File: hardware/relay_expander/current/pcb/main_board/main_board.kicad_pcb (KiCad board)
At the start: 2 copper layers, 100 x 85 mm, 105 parts, among them J1 Conn_01x07_Socket, J10 Screw_Terminal_01x02, J11 Screw_Terminal_01x02, J12 Screw_Terminal_01x02, J13 Screw_Terminal_01x02, J14 Screw_Terminal_01x02, J15 Screw_Terminal_01x02, J2 Conn_01x07_Socket, J3 Screw_Terminal_01x02, J4 Screw_Terminal_01x02, J5 Screw_Terminal_01x02, J6 Screw_Terminal_01x02, J7 Screw_Terminal_01x02, J8 Screw_Terminal_01x03, J9 Screw_Terminal_01x02, K1 HF46F-12-HS1, K2 HF46F-12-HS1, K3 HF46F-12-HS1, K4 HF46F-12-HS1, K5 HF46F-12-HS1, K6 HF46F-12-HS1, K7 HF46F-12-HS1, K8 HF46F-12-HS1, Q1 BC548, Q2 BC548, Q3 BC548, Q4 BC548, Q5 BC548, Q6 BC548, Q7 BC548, Q8 BC548, SW1 SW_DIP_x03, U1 MCP23017x-x-SO, U2 TCMT4100, U3 TCMT4100, U4 TCMT4100, U5 TCMT4100

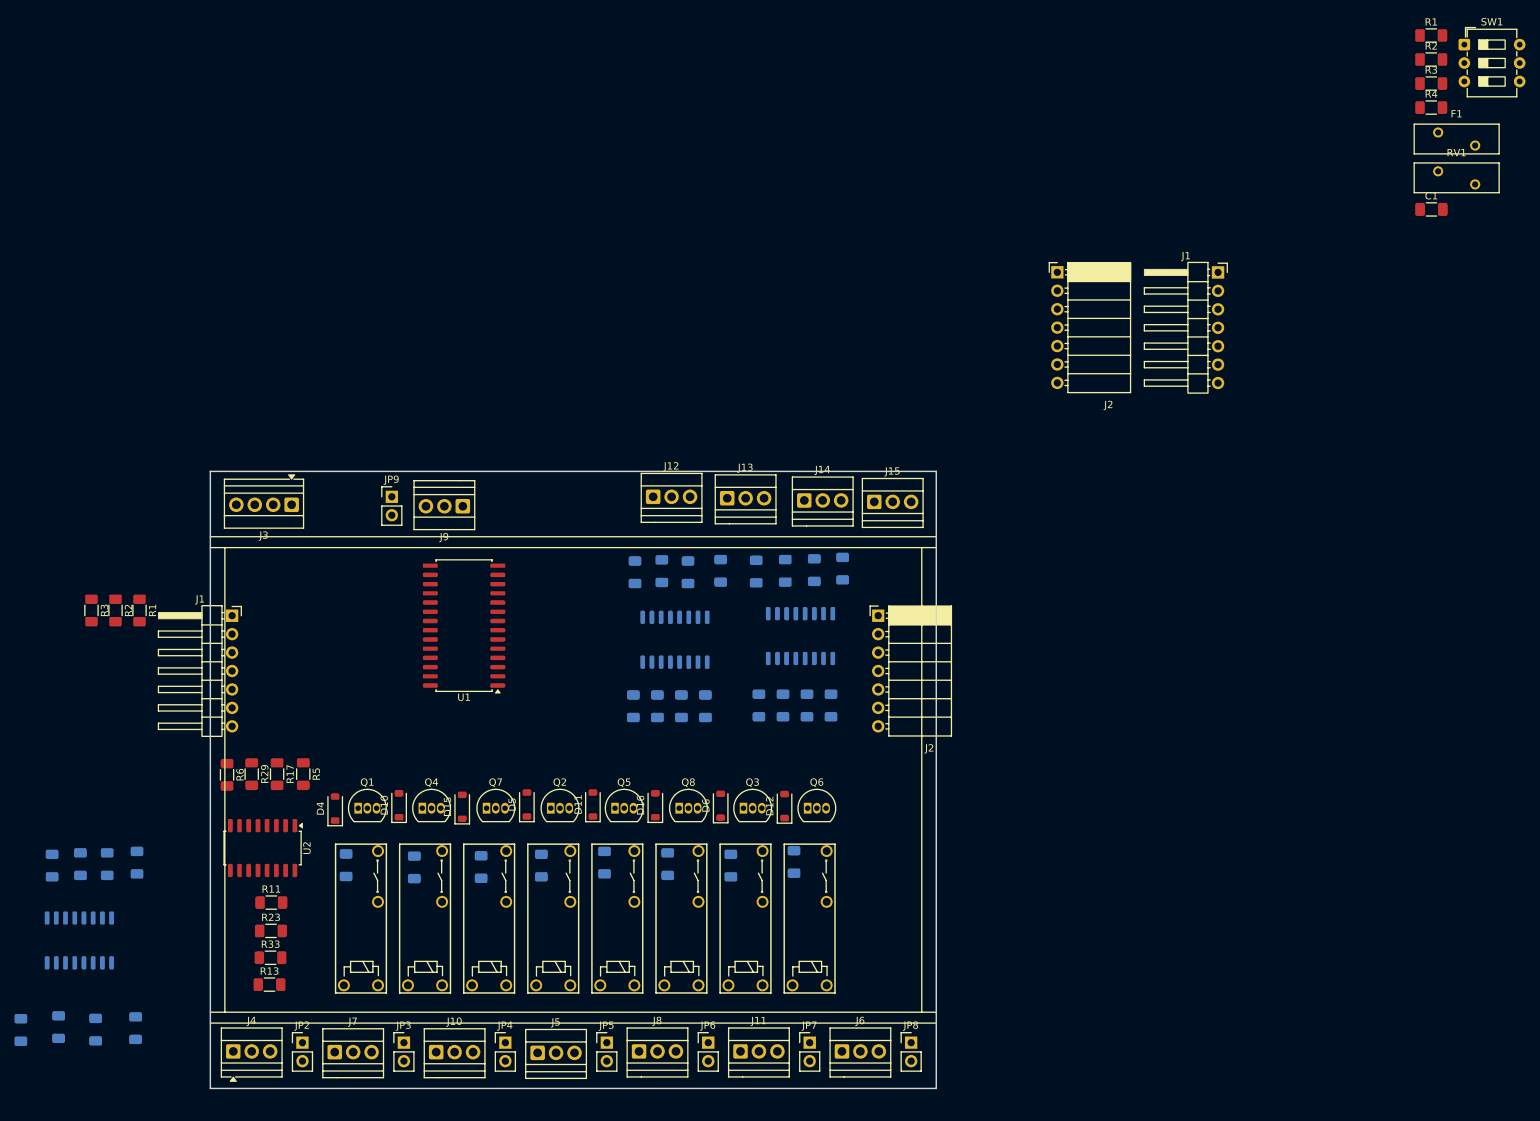
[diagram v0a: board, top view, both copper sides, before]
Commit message: [ADD] ui-board for relay - basic layout
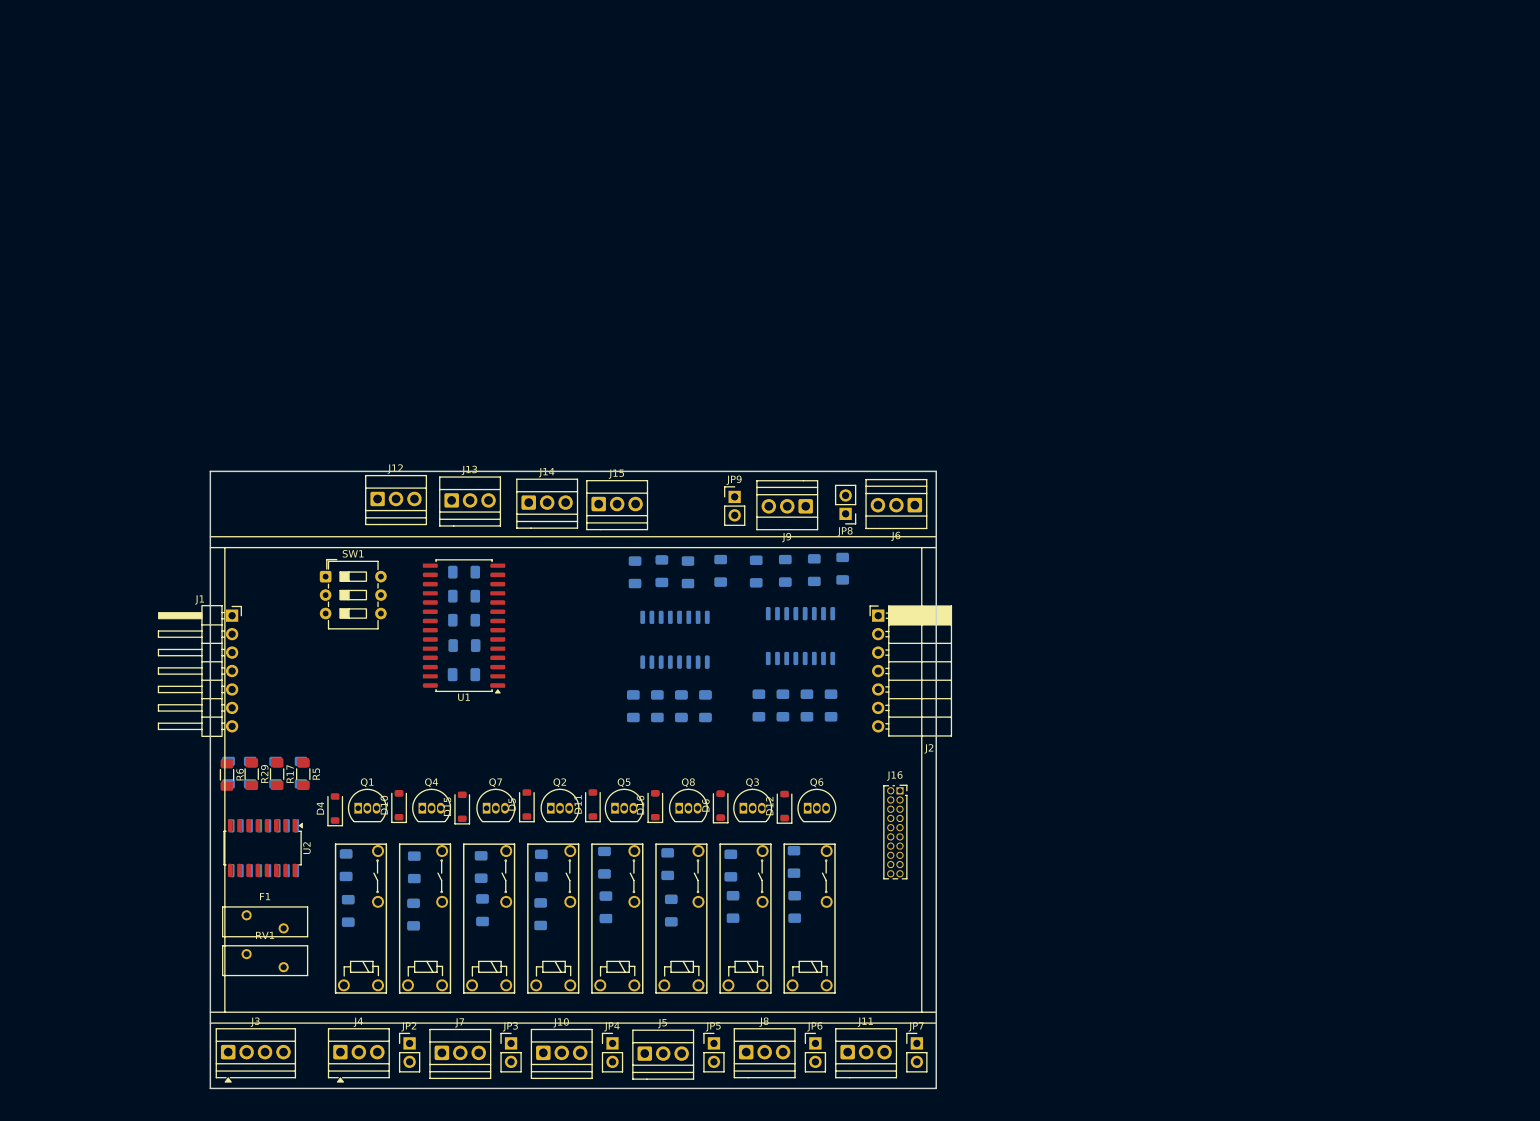
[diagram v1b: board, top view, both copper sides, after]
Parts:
- removed the J1 at (223.8, 32.7)
- removed the J2 at (201.7, 32.7)
- removed the R1 at (75.2, 71.7)
- removed the R1 at (253.2, -7.54)
- removed the R2 at (253.2, -4.24)
- removed the R2 at (71.9, 71.7)
- removed the R3 at (68.6, 71.7)
- removed the R3 at (253.2, -0.93)
- added J16: Conn_01x20_Socket, Connector_PinSocket_1.27mm:PinSocket_2x10_P1.27mm_Vertical, F.Cu at (180.0, 96.5)
- added R1: 10k, Resistor_SMD:R_1206_3216Metric_Pad1.30x1.75mm_HandSolder, B.Cu at (120.0, 76.5)
- added R2: 10k, Resistor_SMD:R_1206_3216Metric_Pad1.30x1.75mm_HandSolder, B.Cu at (120.0, 66.4)
- added R3: 10k, Resistor_SMD:R_1206_3216Metric_Pad1.30x1.75mm_HandSolder, B.Cu at (120.0, 69.7)
- C1, R11, R13, R23, R33, R4: moved to B.Cu
- moved F1 196.4 mm to (90.0, 113.7)
- moved RV1 196.4 mm to (90.0, 119.0)
- moved SW1 173.1 mm to (100.9, 67.0)
- moved R4 150.8 mm to (120.0, 73.0), turned to 180 degrees
- moved C1 147.9 mm to (119.9, 80.5), turned to 180 degrees
- moved R27 92.3 mm to (165.5, 112.5), turned to 90 degrees
- moved R25 91.1 mm to (148.5, 113.0), turned to 90 degrees
- moved R15 89.4 mm to (157.0, 112.5), turned to 90 degrees
- moved R35 77.2 mm to (139.5, 112.5), turned to 90 degrees
- moved J6 75.9 mm to (182.0, 57.1), turned to 180 degrees
- moved J3 75.9 mm to (87.5, 132.5), turned to 0 degrees
- moved JP8 73.4 mm to (172.5, 58.4), turned to 180 degrees
- moved J9 47.2 mm to (167.0, 57.3)
- moved JP9 47.2 mm to (157.2, 56.0)
- moved R13 38.6 mm to (130.5, 113.5), turned to 90 degrees
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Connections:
- net Net-(D1-K) renamed /Relays/LED_RELAY_1
- net Net-(D10-A) renamed /Relays/LED_RELAY_2
- net Net-(D11-A) renamed /Relays/LED_RELAY_5
- net Net-(D12-A) renamed /Relays/LED_RELAY_8
- net Net-(D13-K) renamed /Relays/LED_RELAY_3
- net Net-(D14-K) renamed /Relays/LED_RELAY_6
- net Net-(D2-K) renamed /Relays/LED_RELAY_4
- net Net-(D3-K) renamed /Relays/LED_RELAY_7
- J14 pad 3: GND_2 -> +12V

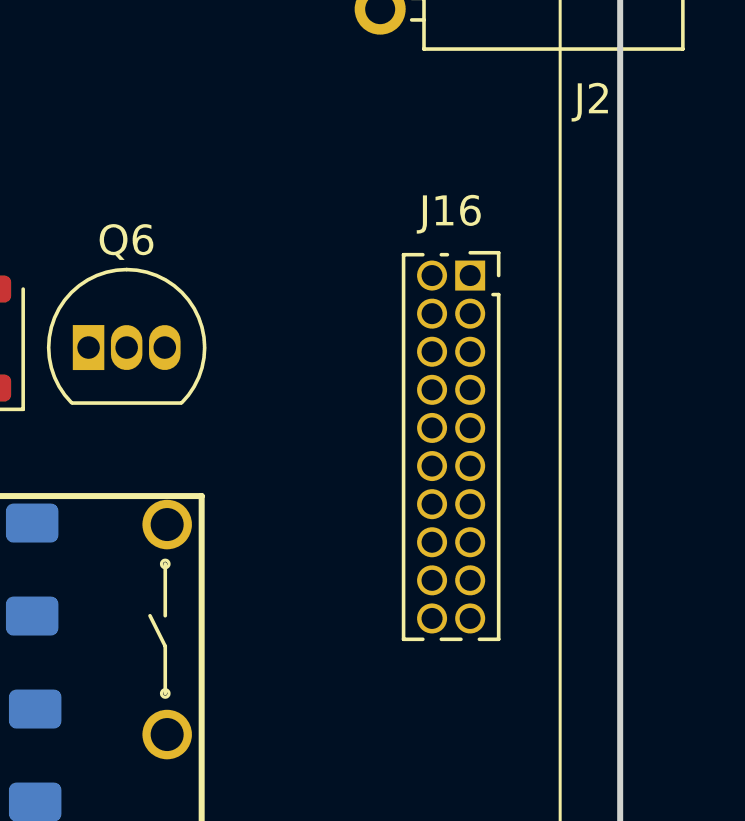
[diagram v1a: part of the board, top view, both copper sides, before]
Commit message: [FIX] problem with connector to expander board
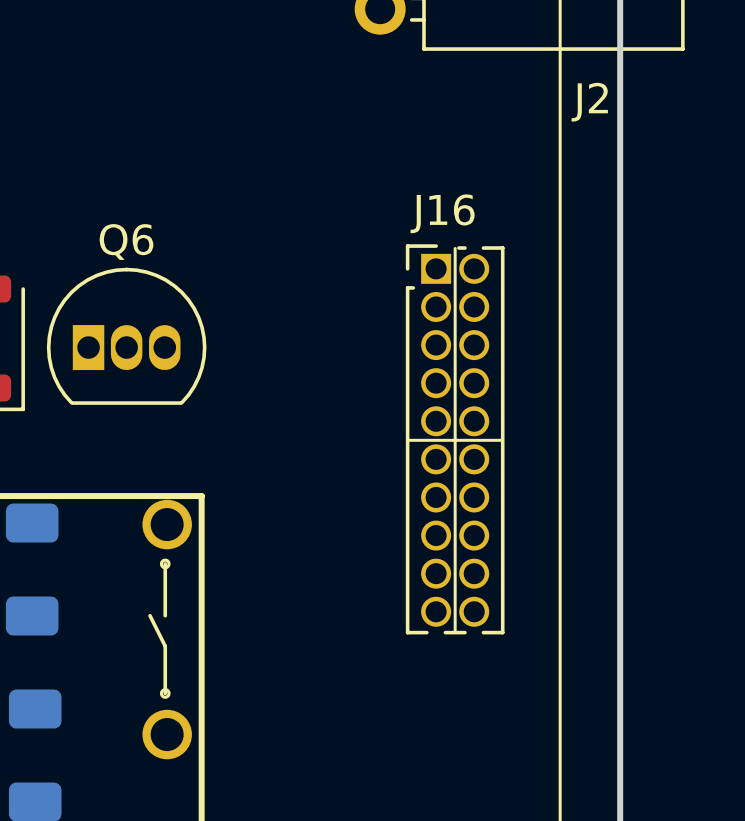
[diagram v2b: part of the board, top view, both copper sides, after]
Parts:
- J16: footprint Connector_PinSocket_1.27mm:PinSocket_2x10_P1.27mm_Vertical -> homeautomation_core:PinSocket_2x10_P1.27mm_Vertical
- moved J16 5.52 mm to (179.5, 102.0)

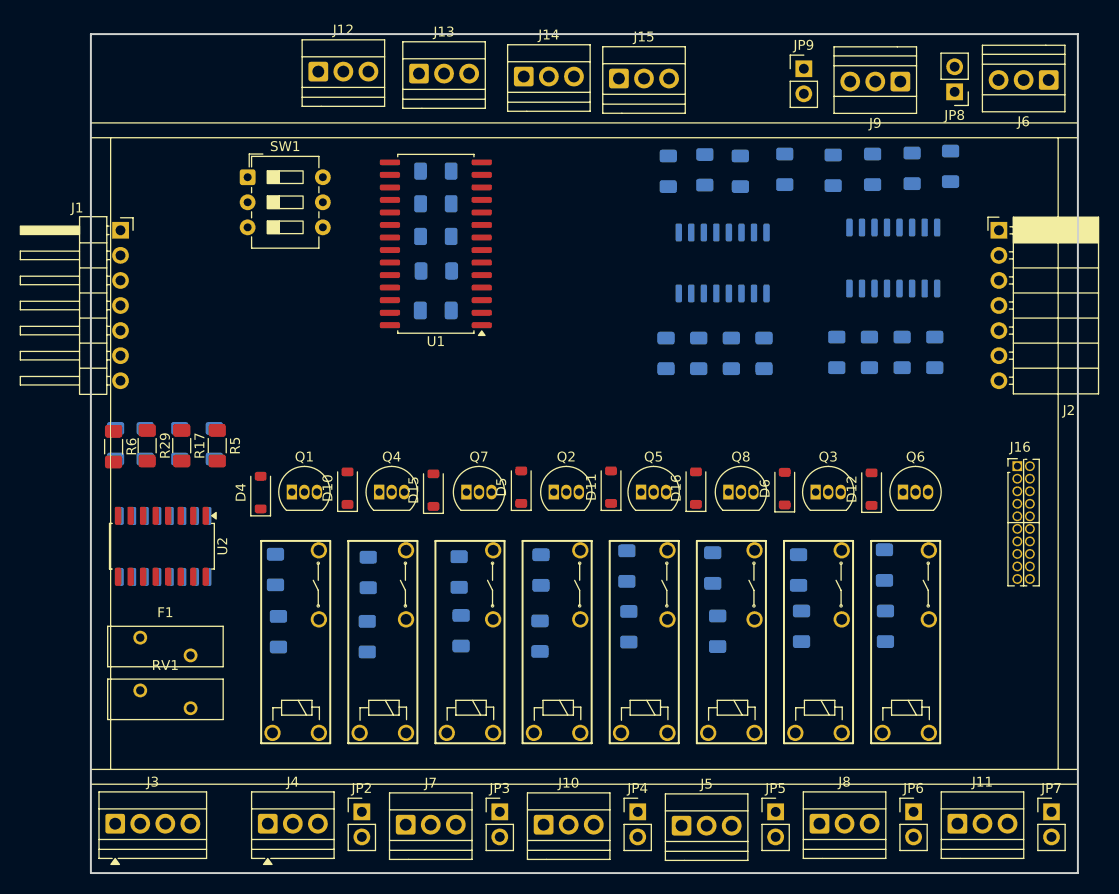
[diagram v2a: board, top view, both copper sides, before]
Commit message: [ADD] board connector
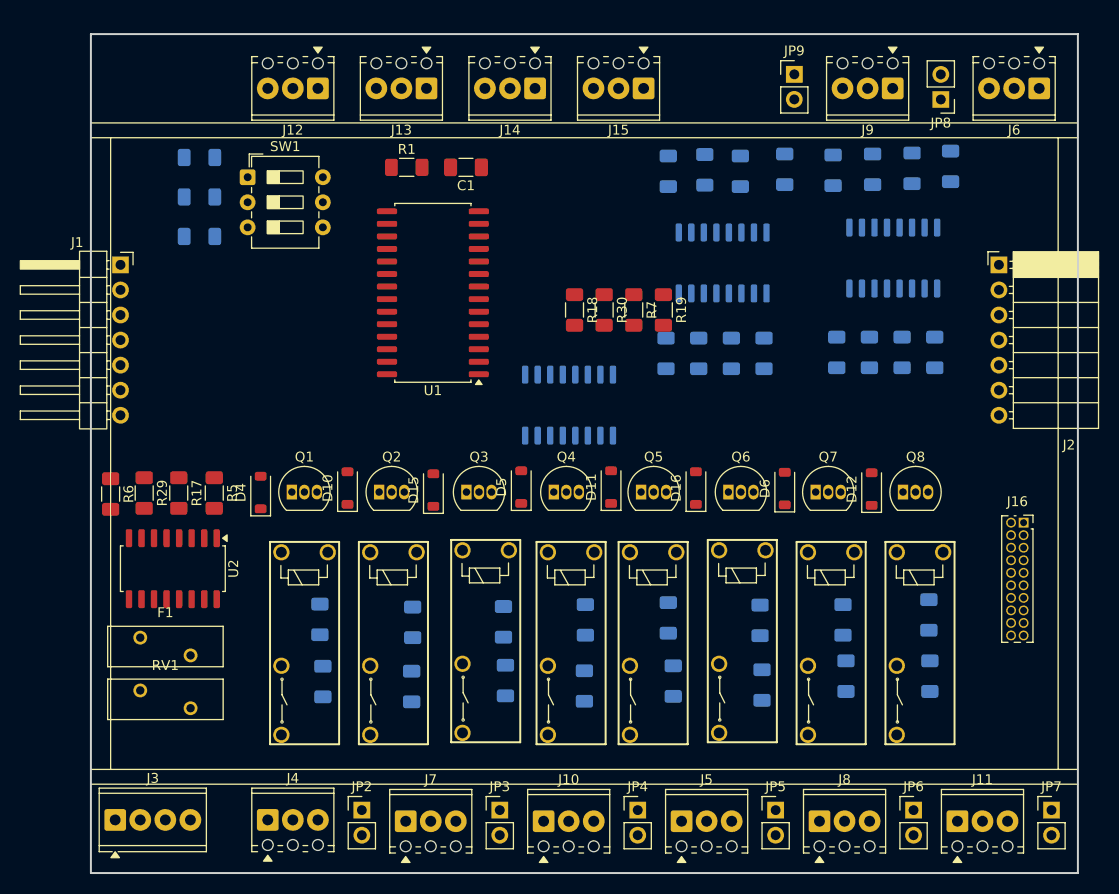
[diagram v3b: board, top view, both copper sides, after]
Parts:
- C1, R1, R18, R19, R30, R7: moved to F.Cu
- J10, J11, J12, J13, J14, J15, J5, J6, J7, J8, J9: footprint footprints:Terminal_block_1x3_2,54 -> TerminalBlock_Phoenix:TerminalBlock_Phoenix_MPT-0,5-3-2.54_1x03_P2.54mm_Horizontal
- J16: footprint homeautomation_core:PinSocket_2x10_P1.27mm_Vertical -> Connector_PinSocket_1.27mm:PinSocket_2x10_P1.27mm_Vertical
- J3: footprint TerminalBlock:TerminalBlock_Xinya_XY308-2.54-4P_1x04_P2.54mm_Horizontal -> TerminalBlock_Phoenix:TerminalBlock_Phoenix_MPT-0,5-4-2.54_1x04_P2.54mm_Horizontal
- J4: footprint TerminalBlock:TerminalBlock_Xinya_XY308-2.54-3P_1x03_P2.54mm_Horizontal -> TerminalBlock_Phoenix:TerminalBlock_Phoenix_MPT-0,5-3-2.54_1x03_P2.54mm_Horizontal
- moved R18 48.4 mm to (134.0, 80.5)
- moved R30 48.4 mm to (137.0, 80.5)
- moved R7 48.0 mm to (140.0, 80.5)
- moved R19 47.5 mm to (143.0, 80.5)
- moved K7 45.2 mm to (162.3, 105.0), turned to -90 degrees
- moved U3 43.4 mm to (133.4, 90.1)
- moved K3 34.4 mm to (127.3, 104.8), turned to -90 degrees
- moved K8 30.0 mm to (171.3, 105.0), turned to -90 degrees
- moved K4 30.0 mm to (136.0, 105.0), turned to -90 degrees
- moved R2 24.0 mm to (96.0, 65.0), turned to 0 degrees
- moved R3 24.0 mm to (96.0, 69.0), turned to 0 degrees
- moved R4 24.0 mm to (96.0, 73.0), turned to 0 degrees
- moved K6 22.0 mm to (153.3, 104.8), turned to -90 degrees
- moved K2 21.8 mm to (118.0, 105.0), turned to -90 degrees
- moved K5 19.1 mm to (144.3, 105.0), turned to -90 degrees
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- renumbered K4 to K2, K7 to K3, K2 to K4, K8 to K6, K3 to K7, K6 to K8, Q4 to Q2, Q7 to Q3, Q2 to Q4, Q8 to Q6, Q3 to Q7, Q6 to Q8
